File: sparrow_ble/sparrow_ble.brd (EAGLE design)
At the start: 46 x 31 mm, 58 parts, among them IC1 SI1145, IC2 TC1262, J3 SMALL_HEADER_5X2, Q3 32768kHz, Q4 FA-128, T1 FDV304P, U1 47491-001, U2 FT232R, U3 NRF51822, U4 SI7020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

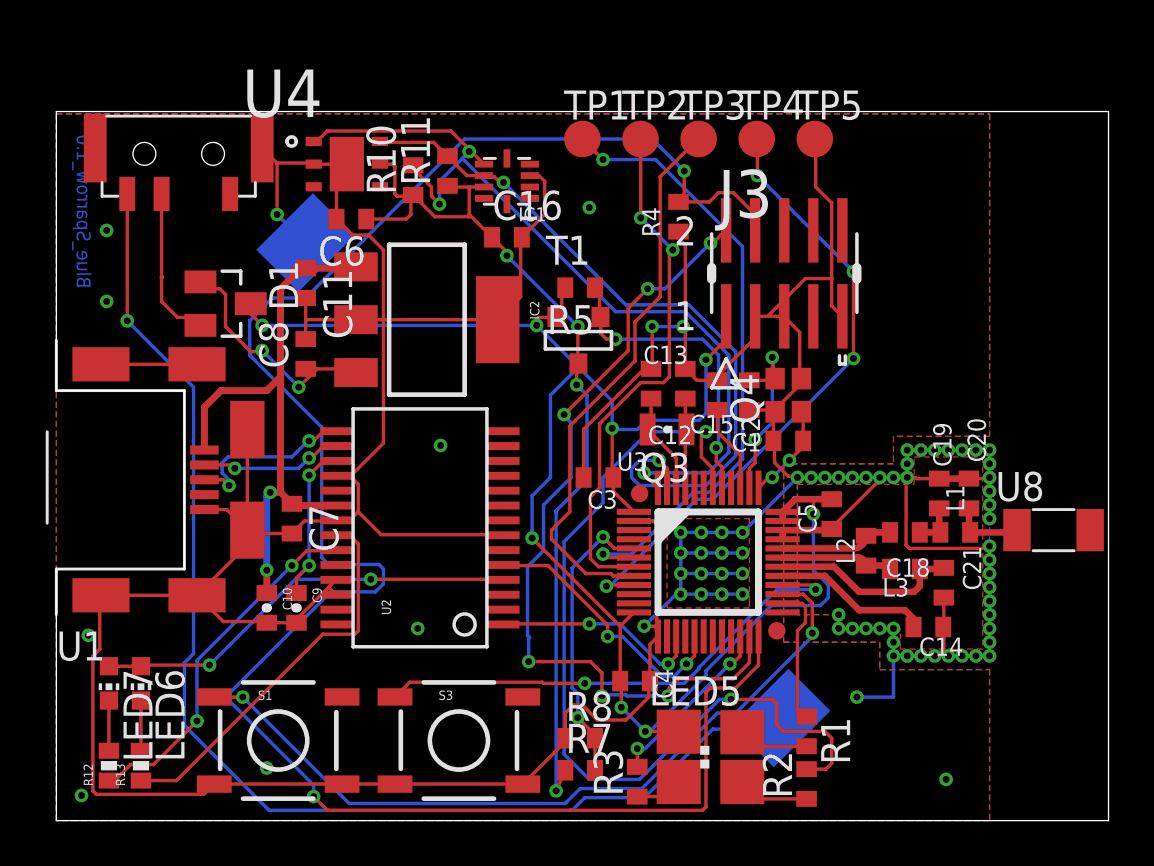
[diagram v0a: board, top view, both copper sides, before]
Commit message: Add new version with fixed balun
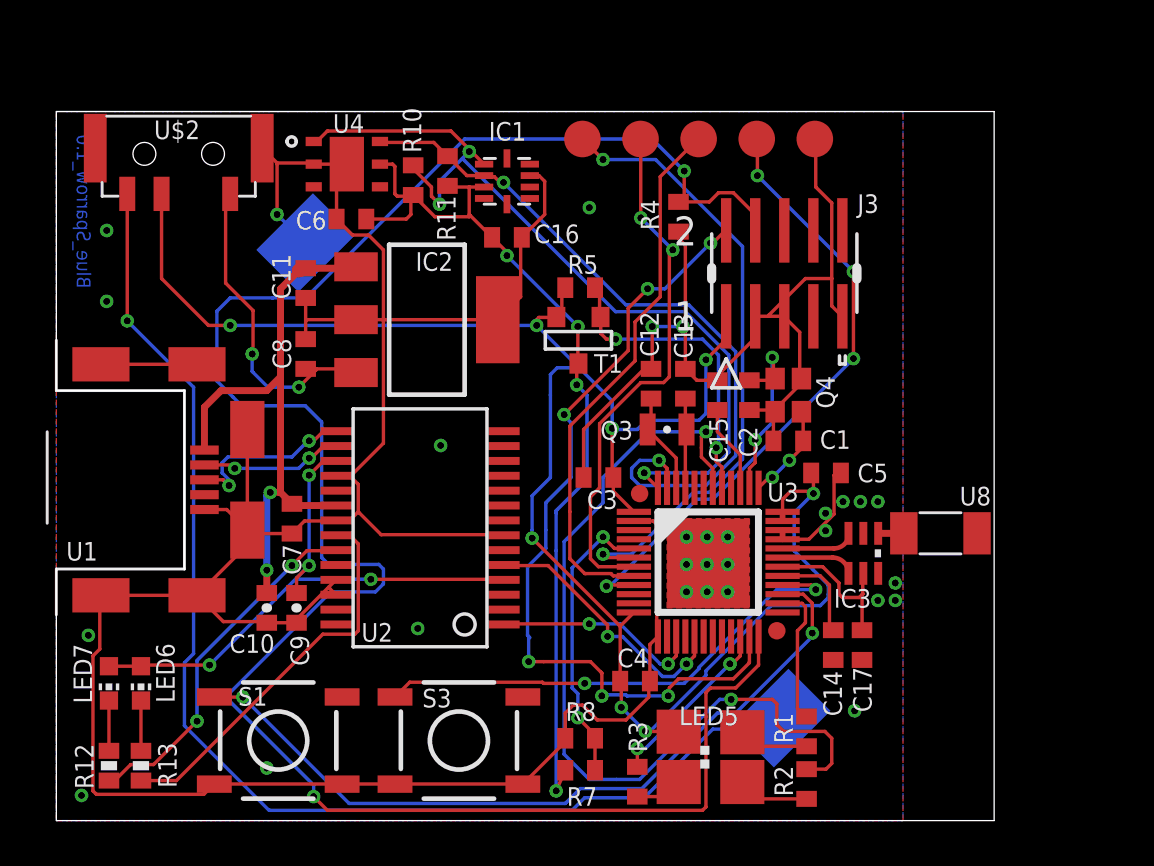
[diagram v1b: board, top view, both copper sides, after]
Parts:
- removed C18: 2.2pF, X7R, resistor:C0402
- removed C19: 1pF, X7R, resistor:C0402
- removed C20: 1.5pF, X7R, resistor:C0402
- removed C21: 2.2nF, X7R, resistor:C0402
- removed D1: BAT54C, diode:SOT23
- removed L1: 3.3nH, SparkFun-Passives:C0402
- removed L2, L3: 4.7nH, HF, SparkFun-Passives:C0402
- added C17: 2,2nF, resistor:C0402
- added F1: 2450BM14E0003, johanson:2450BM15A0002
- IC2: value TC1262 -> TC1262-3.3V
- moved U8 4.95 mm to (38.7, 12.6)
- moved C14 4.23 mm to (34.0, 7.67), turned to 270 degrees
- moved C5 1.82 mm to (33.6, 15.2), turned to 0 degrees
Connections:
- net N$17 renamed VBAT
- removed net N$15: C18.2, C19.2, L1.1
- removed net N$22: C20.2, L1.2, U8.P$1
- removed net N$7: D1.2, U$2.P$2
- removed net N$8: C8.1, D1.1, IC2.3
- new net N$10: F1.1, U8.P$1
- new net VLDO: C8.1, IC2.3, U$2.P$1
- net 3.3V: now also U$2.P$2; no longer D1.3
- net ANT1: now also F1.4; no longer L2.2, L3.1
- net ANT2: now also F1.3; no longer C18.1, L2.1
- net GND: now also C17.2, F1.2, F1.6; no longer C19.1, C20.1, C21.2
- net VDD_PA: now also C17.1, F1.5; no longer C21.1, L3.2
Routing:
- net GND: track 239.4 -> 175.9 mm, vias 75 -> 29
- net VLDO: track 0.00 -> 14.5 mm, vias 0 -> 2
- net 3.3V: track 74.0 -> 84.7 mm
- net N$8: track 10.7 -> 0.00 mm, vias 2 -> 0
- net N$7: track 7.24 -> 0.00 mm
- net SWDCLK: track 85.5 -> 89.4 mm
- net N$22: track 3.16 -> 0.00 mm
- net N$3: track 7.04 -> 4.38 mm
- net N$15: track 1.97 -> 0.00 mm
- net ANT2: track 4.99 -> 3.18 mm
- net ANT1: track 4.91 -> 3.17 mm
- net VDD_PA: track 8.38 -> 6.92 mm
- net N$10: track 0.00 -> 1.44 mm
- net AIN5: track 24.4 -> 23.8 mm
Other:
- board size 46 x 31 mm -> 41 x 31 mm
- board text added: "IC3"
- board text added: "U$2"

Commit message: hw: Update ADC design with values used on actual hardware
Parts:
- R7: value 33k -> 22K
- R8: value 52K3 -> 100K
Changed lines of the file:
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@@
 <?xml version="1.0" encoding="utf-8"?>
 <!DOCTYPE eagle SYSTEM "eagle.dtd">
-<eagle version="6.1">
+<eagle version="7.5.0">
 <drawing>
 <settings>
@@
 </class>
 </classes>
-<designrules>
+<designrules name="default">
 <description language="de">&lt;b&gt;EAGLE Design Rules Prototypen  für PCB-POOL(R)&lt;/b&gt;
 &lt;p&gt;
@@
 <pass name="Default">
 <param name="RoutingGrid" value="0.05mm"/>
+<param name="AutoGrid" value="1"/>
+<param name="Efforts" value="0"/>
+<param name="TopRouterVariant" value="1"/>
 <param name="tpViaShape" value="round"/>
 <param name="PrefDir.1" value="*"/>
@@
 <attribute name="VALUE" x="23.535" y="25.332" size="1.27" layer="27" rot="R180"/>
 </element>
-<element name="R8" library="resistor" package="R0402" value="52K3" x="22.9" y="3.6" smashed="yes">
+<element name="R8" library="resistor" package="R0402" value="100K" x="22.9" y="3.6" smashed="yes">
 <attribute name="NAME" x="22.265" y="4.362" size="0.8128" layer="25"/>
 <attribute name="VALUE" x="22.265" y="1.568" size="1.27" layer="27"/>
 </element>
-<element name="R7" library="resistor" package="R0402" value="33k" x="22.9" y="2.2" smashed="yes">
+<element name="R7" library="resistor" package="R0402" value="22K" x="22.9" y="2.2" smashed="yes">
 <attribute name="NAME" x="22.3158" y="0.6506" size="0.8128" layer="25"/>
 <attribute name="VALUE" x="22.265" y="0.168" size="1.27" layer="27"/>
